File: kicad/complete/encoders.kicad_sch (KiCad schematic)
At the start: 0 parts

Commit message: schematic continued
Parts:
- added SW2: ENC1, EasyEDA_Lib:SW-TH_EC11E1820402, symbol EasyEDA_Lib:EC11E1834403
- added SW3: ENC2, EasyEDA_Lib:SW-TH_EC11E1820402, symbol EasyEDA_Lib:EC11E1834403
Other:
- title: (none) -> bitseithr synth - encoders

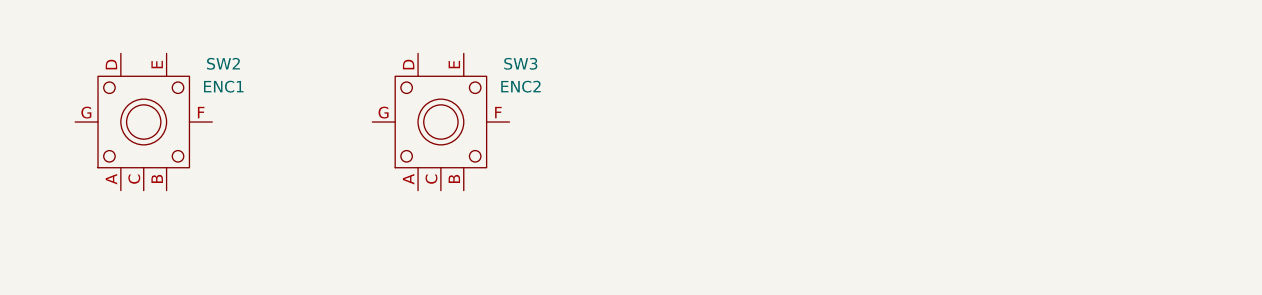
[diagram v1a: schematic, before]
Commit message: saving op-amp config before I mess with the feedback resistor
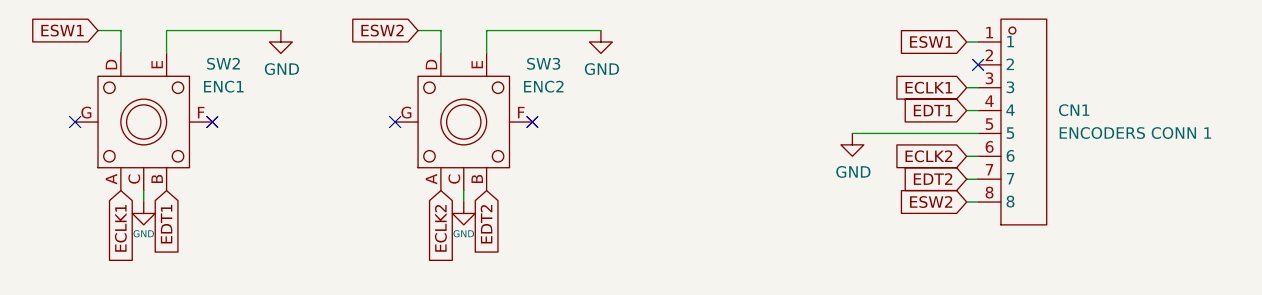
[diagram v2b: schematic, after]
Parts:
- added CN1: ENCODERS CONN 1, EasyEDA_Lib:CONN-TH_8P-P2.50_HCTL_HC-XA-8AW, symbol EasyEDA_Lib:HC-XA-8AW
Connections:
- net ECLK2: now reaches SW3.A
- net ECLK2: now also CN1.6
- net EDT2: now reaches SW3.B
- net EDT2: now also CN1.7
- net GND: now reaches SW3.C
- net GND: now also SW2.C, SW2.E, SW3.E, CN1.5
- net ESW2: now reaches SW3.D
- net ESW2: now also CN1.8
- net ECLK1: now reaches SW2.A
- net ECLK1: now also CN1.3
- net EDT1: now reaches SW2.B
- net EDT1: now also CN1.4
- net ESW1: now reaches SW2.D
- net ESW1: now also CN1.1
- no-connect marks 0 -> 5
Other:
- moved on the sheet: SW3

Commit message: erc and llm review complete
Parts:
- renumbered CN1 to CN13
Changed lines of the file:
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@@
 		(on_board yes)
 		(dnp no)
-		(property "Reference" "#PWR054"
+		(property "Reference" "#PWR061"
 			(at 177.8 81.28 0)
 			(effects
@@
 			(project "bitseithr-complete"
 				(path "/e63e39d7-6ac0-4ffd-8aa3-1841a4541b55/76dd9f28-7dda-49af-8673-8e1a5d555654"
-					(reference "#PWR054")
+					(reference "#PWR061")
 					(unit 1)
 				)
@@
 		(on_board yes)
 		(dnp no)
-		(property "Reference" "#PWR050"
+		(property "Reference" "#PWR059"
 			(at 134.62 88.9 0)
 			(effects
@@
 			(project "bitseithr-complete"
 				(path "/e63e39d7-6ac0-4ffd-8aa3-1841a4541b55/76dd9f28-7dda-49af-8673-8e1a5d555654"
-					(reference "#PWR050")
+					(reference "#PWR059")
 					(unit 1)
 				)
@@
 		(dnp no)
 		(fields_autoplaced yes)
-		(property "Reference" "CN1"
+		(property "Reference" "CN13"
 			(at 200.66 72.3899 0)
 			(effects
@@
 			(project ""
 				(path "/e63e39d7-6ac0-4ffd-8aa3-1841a4541b55/76dd9f28-7dda-49af-8673-8e1a5d555654"
-					(reference "CN1")
+					(reference "CN13")
 					(unit 1)
 				)
@@
 		(on_board yes)
 		(dnp no)
-		(property "Reference" "#PWR051"
+		(property "Reference" "#PWR057"
 			(at 99.06 88.9 0)
 			(effects
@@
 			(project "bitseithr-complete"
 				(path "/e63e39d7-6ac0-4ffd-8aa3-1841a4541b55/76dd9f28-7dda-49af-8673-8e1a5d555654"
-					(reference "#PWR051")
+					(reference "#PWR057")
 					(unit 1)
 				)
@@
 		(on_board yes)
 		(dnp no)
-		(property "Reference" "#PWR053"
+		(property "Reference" "#PWR058"
 			(at 114.3 69.85 0)
 			(effects
@@
 			(project "bitseithr-complete"
 				(path "/e63e39d7-6ac0-4ffd-8aa3-1841a4541b55/76dd9f28-7dda-49af-8673-8e1a5d555654"
-					(reference "#PWR053")
+					(reference "#PWR058")
 					(unit 1)
 				)
@@
 		(on_board yes)
 		(dnp no)
-		(property "Reference" "#PWR052"
+		(property "Reference" "#PWR060"
 			(at 149.86 69.85 0)
 			(effects
@@
 			(project "bitseithr-complete"
 				(path "/e63e39d7-6ac0-4ffd-8aa3-1841a4541b55/76dd9f28-7dda-49af-8673-8e1a5d555654"
-					(reference "#PWR052")
-					(unit 1)
-				)
+					(reference "#PWR060")
+					(unit 1)
+				)
